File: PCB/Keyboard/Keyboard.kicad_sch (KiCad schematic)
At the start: 21 parts, among them J1 USB_C_Receptacle_USB2.0, U1 STM32F072CBT6, U2 PRTR5V0U2X, U3 XC6206PxxxMR-Regulator_Linear

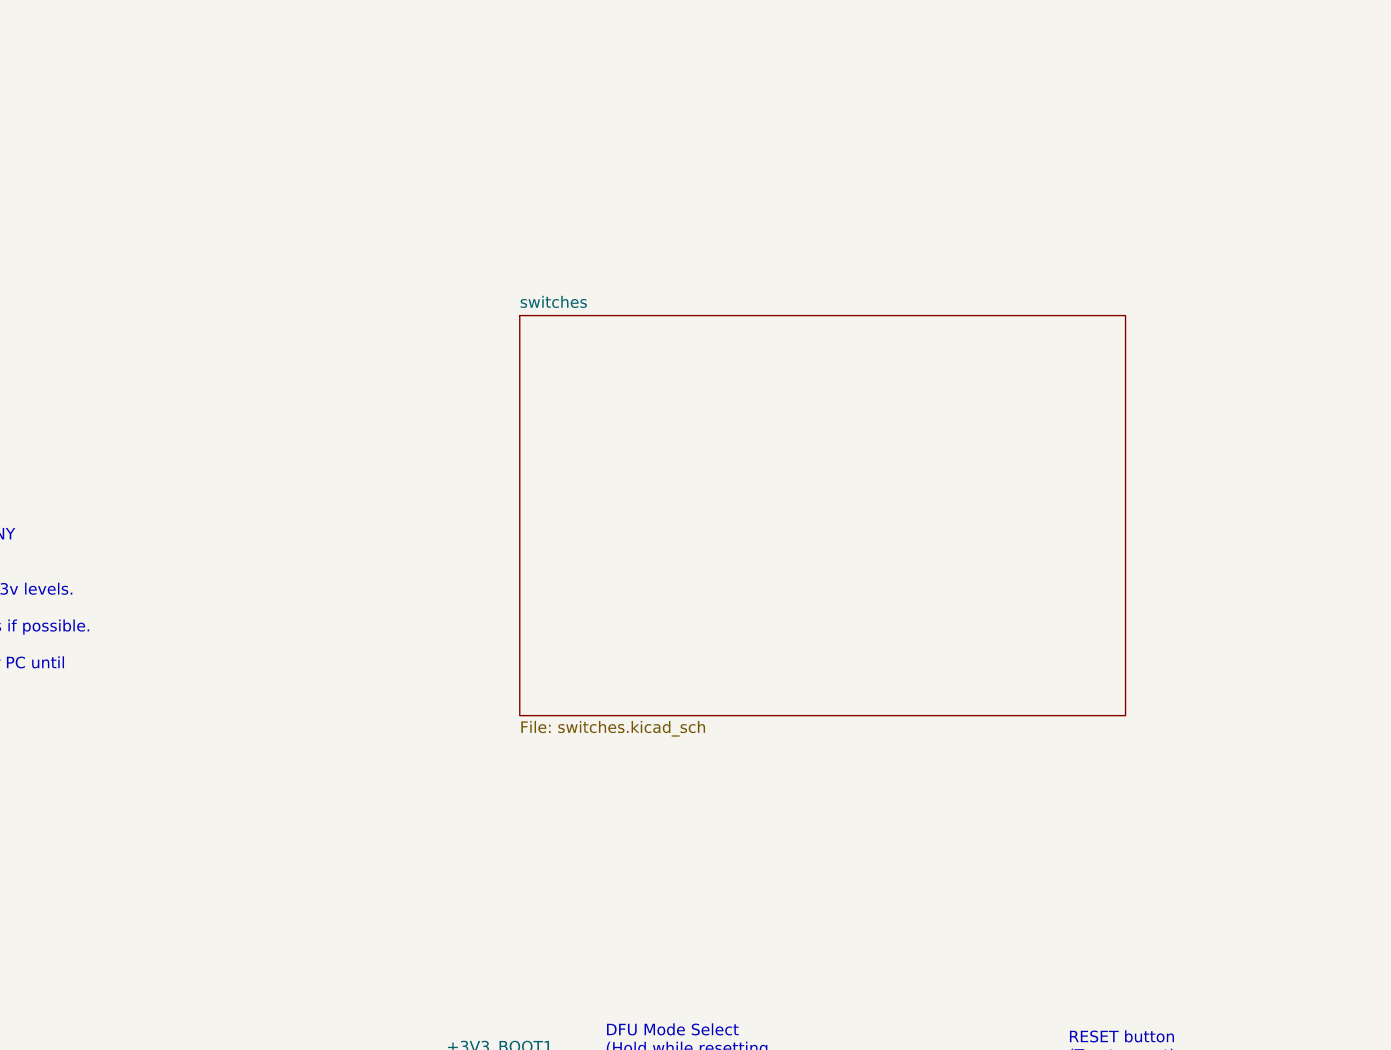
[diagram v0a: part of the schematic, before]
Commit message: wire rows and cols
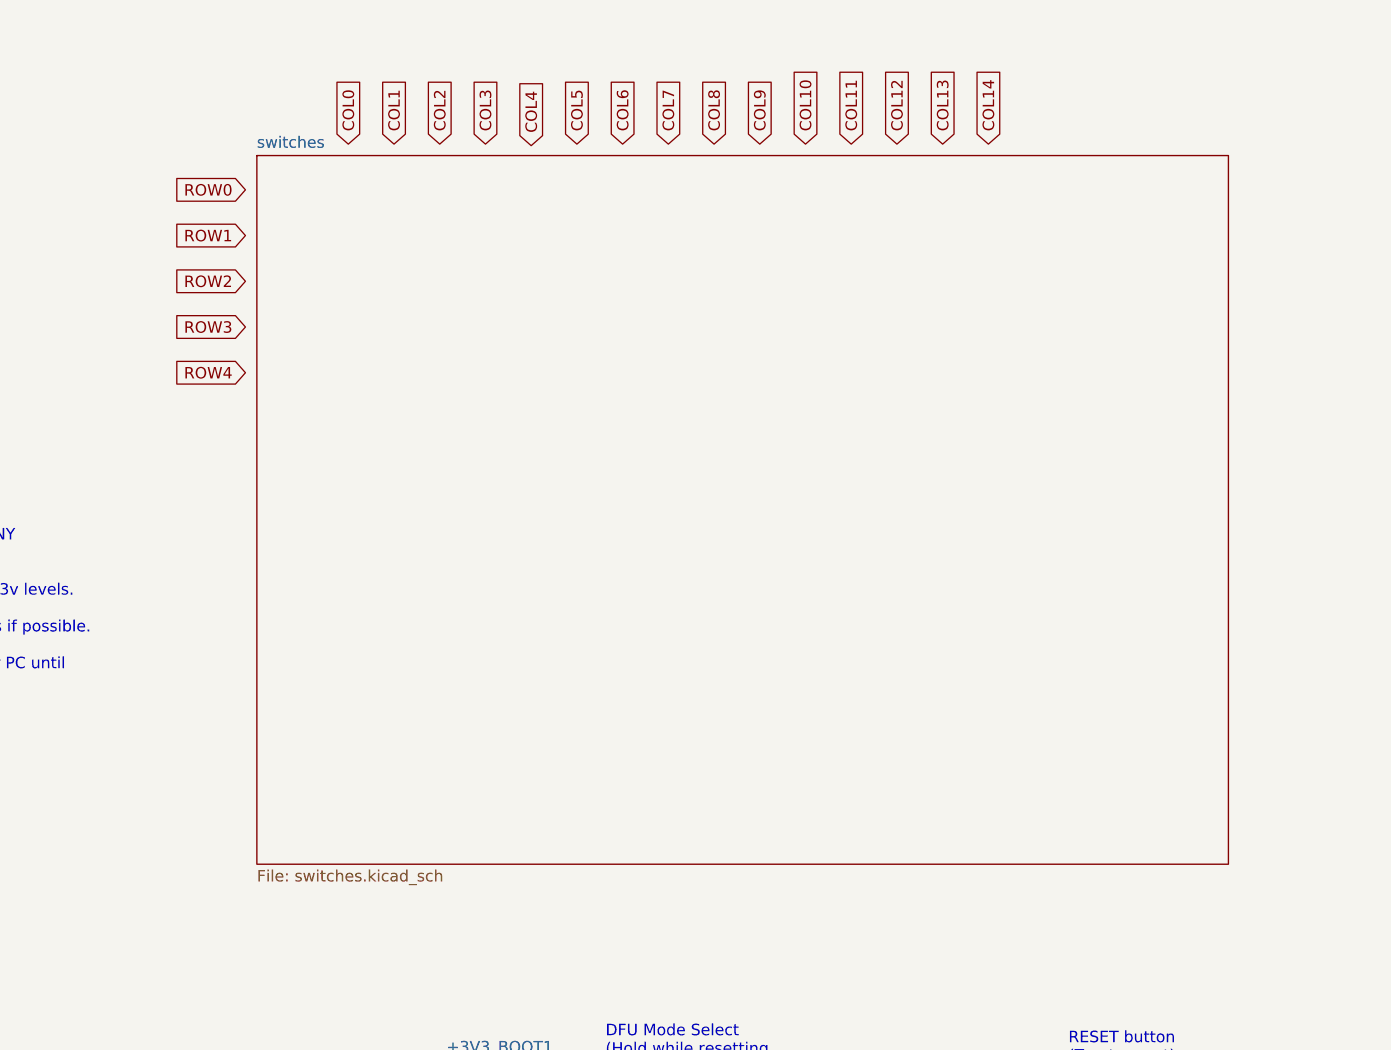
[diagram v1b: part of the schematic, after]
